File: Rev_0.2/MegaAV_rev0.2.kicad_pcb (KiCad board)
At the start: 2 copper layers, 40.4 x 55 mm, 148 parts, among them CN1 MD-90SM_MD2, U1 ICS501, U2 MC33204, U3 THS7374, U4 MC33204, U5 AD725

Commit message: Silkscreen updated.
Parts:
- added G***: LOGO, LOGO_Library:RIP-Felix Logo(Small), B.Cu at (258.5, 114.0)
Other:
- board text added: "+"
- board text added: "Dev Team: villahed94 ACE9921 RGBeter"
- board text added: "Jumper Settings"
- board text added: "M1 PU"
- board text added: "M1va0-6.5 = 1"
- board text added: "M1va0-6.5 = 1, M1PU M1va7 = 2, c, d-right, e, M1PU"
- board text added: "M1va7 - M2va0-1.8, M2va3 = 2"
- board text added: "M2Va4, M3va2 = 3, PSG-Right"
- board text added: "M2va0-1.8 = 2, c, d-right, e M2Va3 = 2 M2va2-2.3 = 1, d-left M2va4 = 3, d-right"
- board text added: "M2va2-2.3 = 1, PSG-Left"
- board text added: "M3 = 3, b, c, d-right, e, f"
- board text added: "M3va1 = 3, CD_R, 32x_R, PSG-Right, 32x_L, CD_L"
- board text added: "Original Design: dbElectronics"
- board text added: "PAL: PAL=Short"
- board text added: "R"
- board text added: "RGB lifted: M1PU"
- board text added: "RIP-Felix"
- board text added: "S75"
- board text added: "S75 = 75 Ohm CSYNC to Pin 4"
- board text added: "SL"
- board text added: "SR"
- board text added: "STTL"
- board text added: "TRIPLE BYPASS V2A"
- board text added: "Updated Design:"

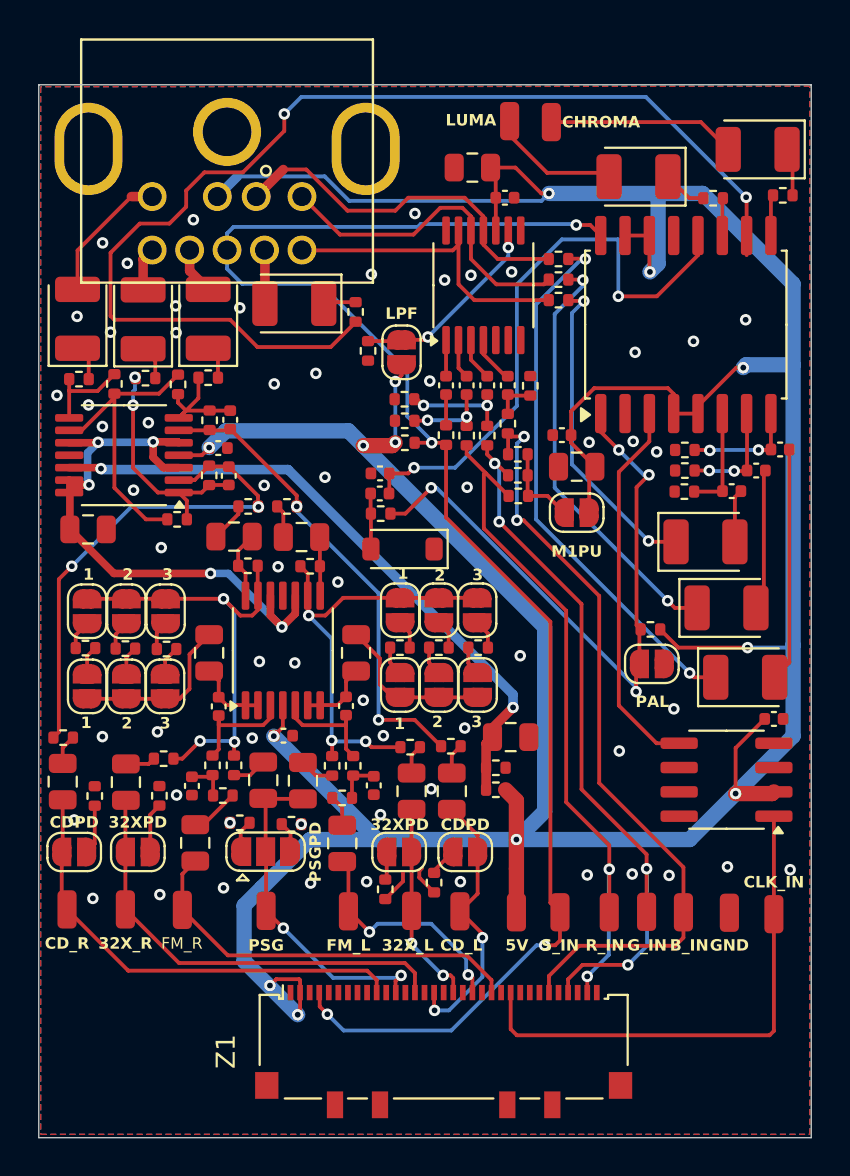
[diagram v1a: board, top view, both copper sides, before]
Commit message: fixed silkscreening, minor trace rerouting, and added PCBA files. Note, these are not final.
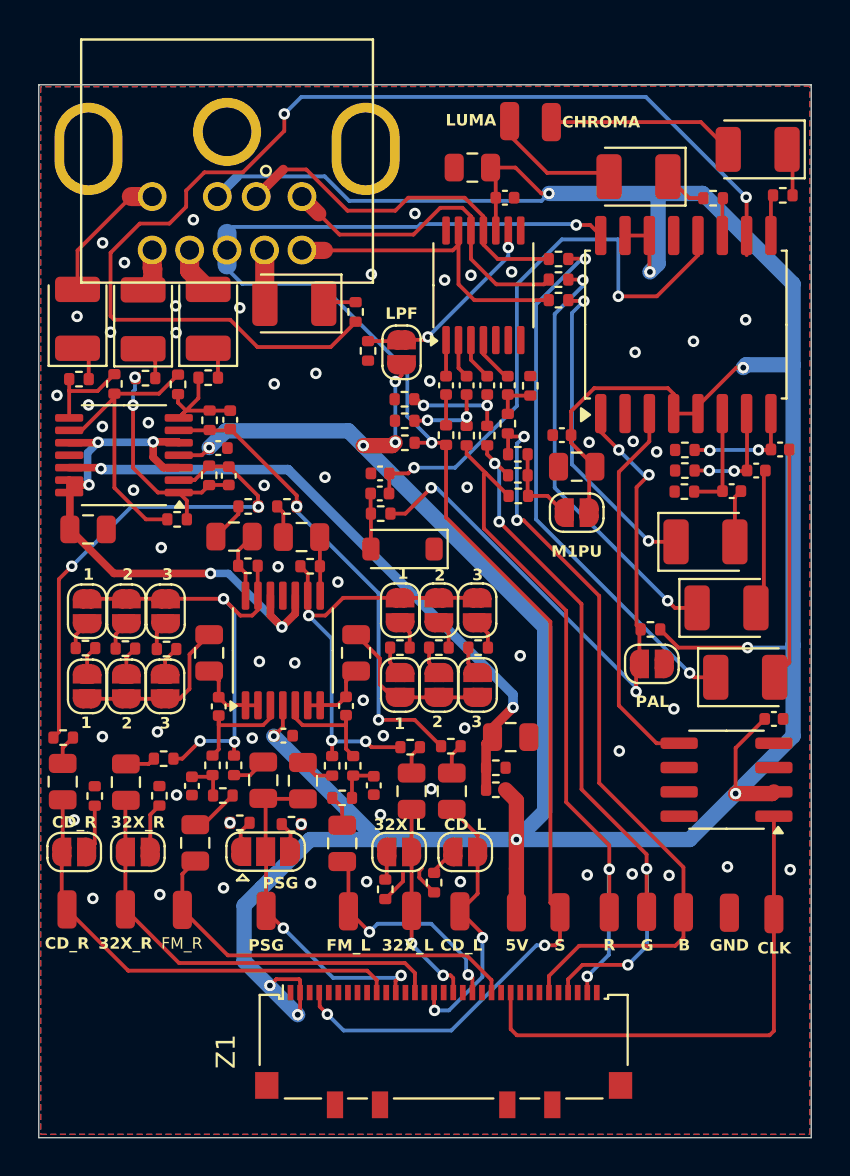
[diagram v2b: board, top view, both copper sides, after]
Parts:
- renumbered 32XPD to 32X_L, 32XPD to 32X_R, B_IN to B, CDPD to CD_L, CDPD to CD_R, CLK_IN to CLK, G_IN to G, PSGPD to PSG, R_IN to R, S_IN to S
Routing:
- net /CSync: track 83.5 -> 84.3 mm
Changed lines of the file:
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@@
 			(outputformat 1)
 			(mirror no)
-			(drillshape 1)
+			(drillshape 0)
 			(scaleselection 1)
-			(outputdirectory "")
+			(outputdirectory "PCBA Files/Gerber/")
 		)
 	)
@@
 		(descr "Wire Pad, Square, SMD Pad,  1mm x 2mm,")
 		(tags "MesurementPoint Square SMDPad 1mmx2mm ")
-		(property "Reference" "G_IN"
+		(property "Reference" "G"
 			(at 0.025 1.75 0)
 			(layer "F.SilkS")
@@
 		(descr "SMD Solder Jumper, 1x1.5mm, rounded Pads, 0.3mm gap, open")
 		(tags "solder jumper open")
-		(property "Reference" "CDPD"
+		(property "Reference" "CD_R"
 			(at 0 1.55 0)
 			(layer "F.SilkS")
@@
 		(descr "Wire Pad, Square, SMD Pad,  1mm x 2mm,")
 		(tags "MesurementPoint Square SMDPad 1mmx2mm ")
-		(property "Reference" "CLK_IN"
-			(at 0 -1.675 0)
+		(property "Reference" "CLK"
+			(at 0.015 1.775 0)
 			(layer "F.SilkS")
 			(effects
@@
 		(descr "Wire Pad, Square, SMD Pad,  1mm x 2mm,")
 		(tags "MesurementPoint Square SMDPad 1mmx2mm ")
-		(property "Reference" "S_IN"
+		(property "Reference" "S"
 			(at 0 1.725 0)
 			(layer "F.SilkS")
@@
 		(descr "Wire Pad, Square, SMD Pad,  1mm x 2mm,")
 		(tags "MesurementPoint Square SMDPad 1mmx2mm ")
-		(property "Reference" "B_IN"
-			(at 0.3 1.725 0)
+		(property "Reference" "B"
+			(at 0.04 1.715 0)
 			(layer "F.SilkS")
 			(effects
@@
 		(descr "SMD Solder 3-pad Jumper, 1x1.5mm rounded Pads, 0.3mm gap, open")
 		(tags "solder jumper open")
-		(property "Reference" "PSGPD"
-			(at 2.6 0.0175 90)
+		(property "Reference" "PSG"
+			(at 0.775 1.6425 180)
 			(layer "F.SilkS")
 			(effects
@@
 		(descr "Wire Pad, Square, SMD Pad,  1mm x 2mm,")
 		(tags "MesurementPoint Square SMDPad 1mmx2mm ")
-		(property "Reference" "R_IN"
-			(at -0.225 1.725 0)
+		(property "Reference" "R"
+			(at 0.005 1.715 0)
 			(layer "F.SilkS")
 			(effects
@@
 		(descr "SMD Solder Jumper, 1x1.5mm, rounded Pads, 0.3mm gap, open")
 		(tags "solder jumper open")
-		(property "Reference" "32XPD"
+		(property "Reference" "32X_R"
 			(at 0 -1.55 0)
 			(layer "F.SilkS")
@@
 		(descr "SMD Solder Jumper, 1x1.5mm, rounded Pads, 0.3mm gap, open")
 		(tags "solder jumper open")
-		(property "Reference" "32XPD"
+		(property "Reference" "32X_L"
 			(at 0.025 -1.425 0)
 			(layer "F.SilkS")
@@
 		(descr "SMD Solder Jumper, 1x1.5mm, rounded Pads, 0.3mm gap, open")
 		(tags "solder jumper open")
-		(property "Reference" "CDPD"
+		(property "Reference" "CD_L"
 			(at 0 -1.425 0)
 			(layer "F.SilkS")
@@
 	)
 	(via
-		(at 227.45 111.475)
+		(at 234.6 123.075)
 		(size 0.6)
 		(drill 0.3)
@@
 	)
 	(via
-		(at 234.6 123.075)
+		(at 225.425 118.875)
 		(size 0.6)
 		(drill 0.3)
@@
 	)
 	(via
-		(at 225.425 118.875)
+		(at 227.3 111.44)
 		(size 0.6)
 		(drill 0.3)
@@
 	)
 	(segment
-		(start 234.6375 113.575)
+		(start 234.63 110.8114)
 		(end 234.6375 110.8039)
-		(width 0.5)
+		(width 1)
+		(layer "F.Cu")
+		(net 31)
+	)
+	(segment
+		(start 234.6375 113.575)
+		(end 234.63 113.5675)
+		(width 1)
+		(layer "F.Cu")
+		(net 31)
+	)
+	(segment
+		(start 234.63 113.5675)
+		(end 234.63 110.8114)
+		(width 1)
 		(layer "F.Cu")
 		(net 31)
@@
 	)
 	(segment
+		(start 237.75 110.801)
+		(end 244.448999 110.801)
+		(width 0.2)
+		(layer "F.Cu")
+		(net 38)
+	)
+	(segment
 		(start 244.75 110.499999)
 		(end 244.75 109.7625)
@@
 	)
 	(segment
-		(start 244.448999 110.801)
-		(end 244.75 110.499999)
+		(start 245.575 113.4)
+		(end 249.465 113.4)
 		(width 0.2)
 		(layer "F.Cu")
@@
 	)
 	(segment
-		(start 245.575 113.4)
-		(end 249.465 113.4)
+		(start 244.448999 110.801)
+		(end 244.75 110.499999)
 		(width 0.2)
 		(layer "F.Cu")
@@
 	(segment
 		(start 236.5904 110.801)
-		(end 244.448999 110.801)
-		(width 0.2)
+		(end 237.75 110.801)
+		(width 0.9)
 		(layer "F.Cu")
 		(net 38)
@@
 	)
 	(segment
-		(start 242.4 109.975)
-		(end 243.8 108.575)
-		(width 0.2)
-		(layer "F.Cu")
-		(net 39)
-	)
-	(segment
 		(start 244.949999 108.575)
 		(end 245.4 109.025001)
@@
 	)
 	(segment
-		(start 238.5584 109.975)
-		(end 242.4 109.975)
+		(start 242.4 109.975)
+		(end 243.8 108.575)
 		(width 0.2)
 		(layer "F.Cu")
@@
 	)
 	(segment
+		(start 237.45 108.89)
+		(end 238.535 109.975)
+		(width 0.2)
+		(layer "F.Cu")
+		(net 39)
+	)
+	(segment
+		(start 245.4 109.025001)
+		(end 245.4 109.7625)
+		(width 0.2)
+		(layer "F.Cu")
+		(net 39)
+	)
+	(segment
+		(start 236.5726 108.0126)
+		(end 237.45 108.89)
+		(width 0.8)
+		(layer "F.Cu")
+		(net 39)
+	)
+	(segment
 		(start 243.8 108.575)
 		(end 244.949999 108.575)
@@
 	(segment
 		(start 236.5726 107.9892)
-		(end 238.5584 109.975)
-		(width 0.2)
+		(end 236.5726 108.0126)
+		(width 0.8)
 		(layer "F.Cu")
 		(net 39)
@@
 	)
 	(segment
-		(start 245.4 109.025001)
-		(end 245.4 109.7625)
+		(start 238.535 109.975)
+		(end 242.4 109.975)
 		(width 0.2)
 		(layer "F.Cu")
@@
 	)
 	(segment
-		(start 242.624943 109.575)
-		(end 242.774943 109.425)
+		(start 232.661 109.914)
+		(end 233 109.575)
 		(width 0.2)
 		(layer "B.Cu")
@@
 	)
 	(segment
+		(start 250.85 109.425)
+		(end 250.9 109.475)
+		(width 0.2)
+		(layer "B.Cu")
+		(net 47)
+	)
+	(segment
 		(start 243.35 120.741803)
 		(end 242.075 119.466803)
@@
 	)
 	(segment
-		(start 233 109.575)
-		(end 242.624943 109.575)
-		(width 0.2)
-		(layer "B.Cu")
-		(net 47)
-	)
-	(segment
 		(start 237.525 112.55)
 		(end 233.45 112.55)
@@
 	)
 	(segment
-		(start 232.661 110.7832)
-		(end 232.661 109.914)
+		(start 242.774943 109.425)
+		(end 250.85 109.425)
 		(width 0.2)
 		(layer "B.Cu")
@@
 	)
 	(segment
-		(start 250.85 109.425)
-		(end 250.9 109.475)
+		(start 233 109.575)
+		(end 242.624943 109.575)
 		(width 0.2)
 		(layer "B.Cu")
@@
 	)
 	(segment
-		(start 242.774943 109.425)
-		(end 250.85 109.425)
-		(width 0.2)
+		(start 232.661 111.56)
+		(end 232.661 109.914)
+		(width 1)
 		(layer "B.Cu")
 		(net 47)
@@
 	)
 	(segment
-		(start 232.661 109.914)
-		(end 233 109.575)
+		(start 242.624943 109.575)
+		(end 242.774943 109.425)
 		(width 0.2)
 		(layer "B.Cu")
@@
 	)
 	(segment
-		(start 228.275 111.2576)
+		(start 228.7494 111.732)
 		(end 228.7494 110.7832)
-		(width 0.5)
+		(width 1)
+		(layer "F.Cu")
+		(net 69)
+	)
+	(segment
+		(start 228.78 112.3575)
+		(end 228.78 111.7626)
+		(width 1)
+		(layer "F.Cu")
+		(net 69)
+	)
+	(segment
+		(start 228.78 111.7626)
+		(end 228.7494 111.732)
+		(width 1)
 		(layer "F.Cu")
 		(net 69)
@@
 	(segment
 		(start 228.275 112.8625)
-		(end 228.275 111.2576)
-		(width 0.5)
+		(end 228.78 112.3575)
+		(width 1)
 		(layer "F.Cu")
 		(net 69)
@@
 	)
 	(segment
-		(start 231.675 112.8375)
-		(end 230.7052 111.8677)
-		(width 0.5)
+		(start 230.7052 111.8677)
+		(end 230.7052 110.7832)
+		(width 1)
 		(layer "F.Cu")
 		(net 71)
 	)
 	(segment
-		(start 230.7052 111.8677)
-		(end 230.7052 110.7832)
-		(width 0.5)
+		(start 231.675 112.8375)
+		(end 230.7052 111.8677)
+		(width 1)
 		(layer "F.Cu")
 		(net 71)
@@
 		(start 227.6608 107.9892)
 		(end 228.7494 107.9892)
-		(width 0.5)
+		(width 1)
 		(layer "F.Cu")
 		(net 74)

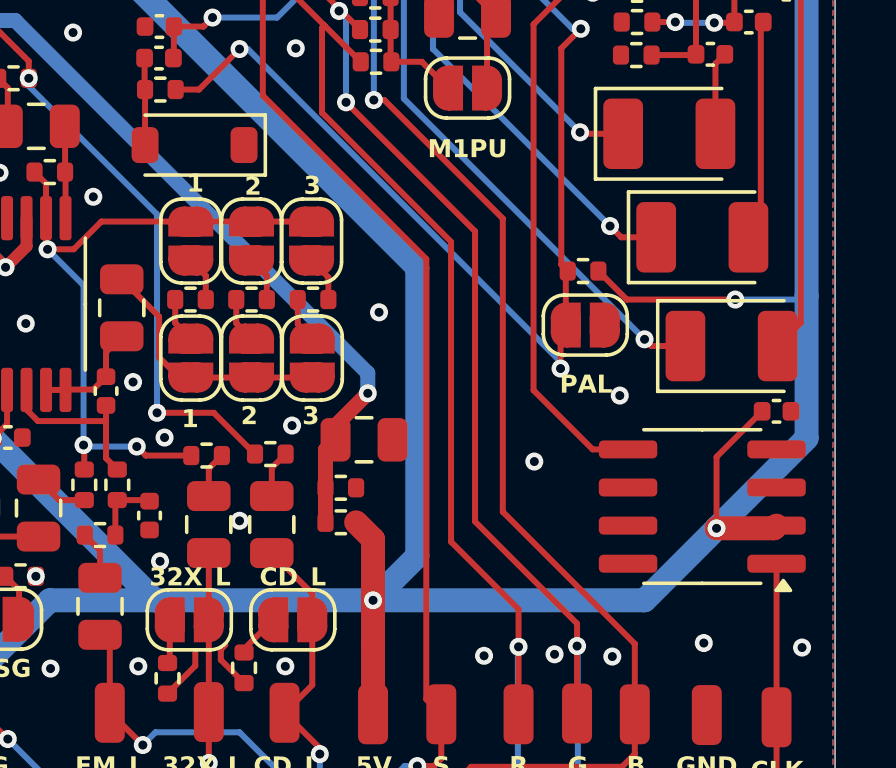
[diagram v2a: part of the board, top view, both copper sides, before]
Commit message: Added MegaAV logo
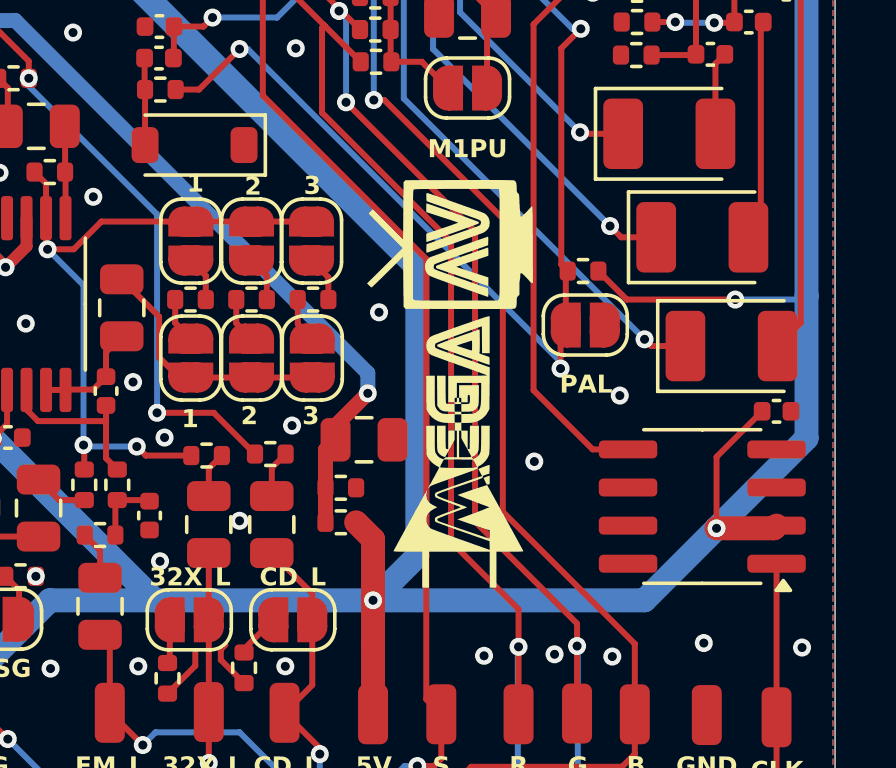
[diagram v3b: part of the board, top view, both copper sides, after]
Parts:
- added G***: LOGO, LOGO_Library:MegaAV Logo 2, F.Cu at (281.7, 119.3)
- added G***: LOGO, LOGO_Library:MegaAV Logo (Small), F.Cu at (250.1, 133.9)
- added G***: LOGO, LOGO_Library:MegaAV Logo 2, B.Cu at (242.2, 147.3)

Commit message: Changes to the liscense, readme, and silkscreening.
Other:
- board text added: "Dev Team: villahed94 RGBeter"
- board text removed: "Dev Team: villahed94 ACE9921 RGBeter"
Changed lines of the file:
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@@
 		)
 	)
-	(gr_text "Dev Team:\nvillahed94\nACE9921\nRGBeter\n"
+	(gr_text "Dev Team:\nvillahed94\nRGBeter\n"
 		(at 261.25 106.75 0)
 		(layer "B.SilkS")
